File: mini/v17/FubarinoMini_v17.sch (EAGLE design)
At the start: 37 parts, among them IC1 AZ1117CR2-3.3TRG1, J1 M20, J2 M20, J8 USB-5PIN, Q1 8MHz, Q2 32.768 KHz, U1 PIC32MX270F256D_44QFN_44

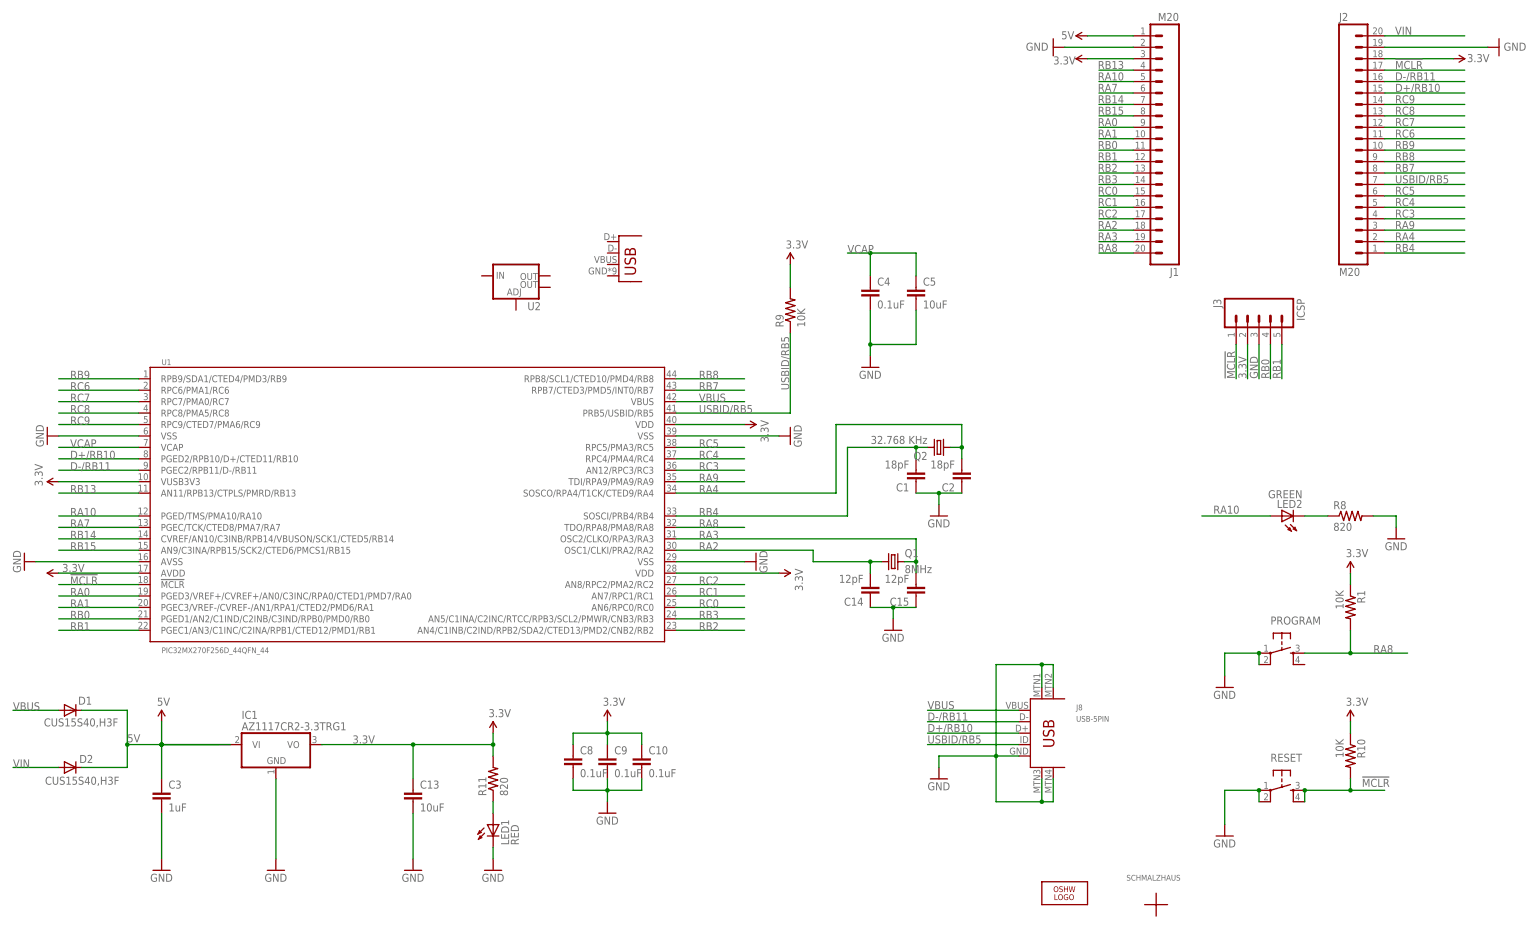
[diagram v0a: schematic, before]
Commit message: Version 2.0, first draft, done and sent to PCB fab. Changed switches, crystal, USB connector, rerouted most of board. Still need to rename folder to 2.0
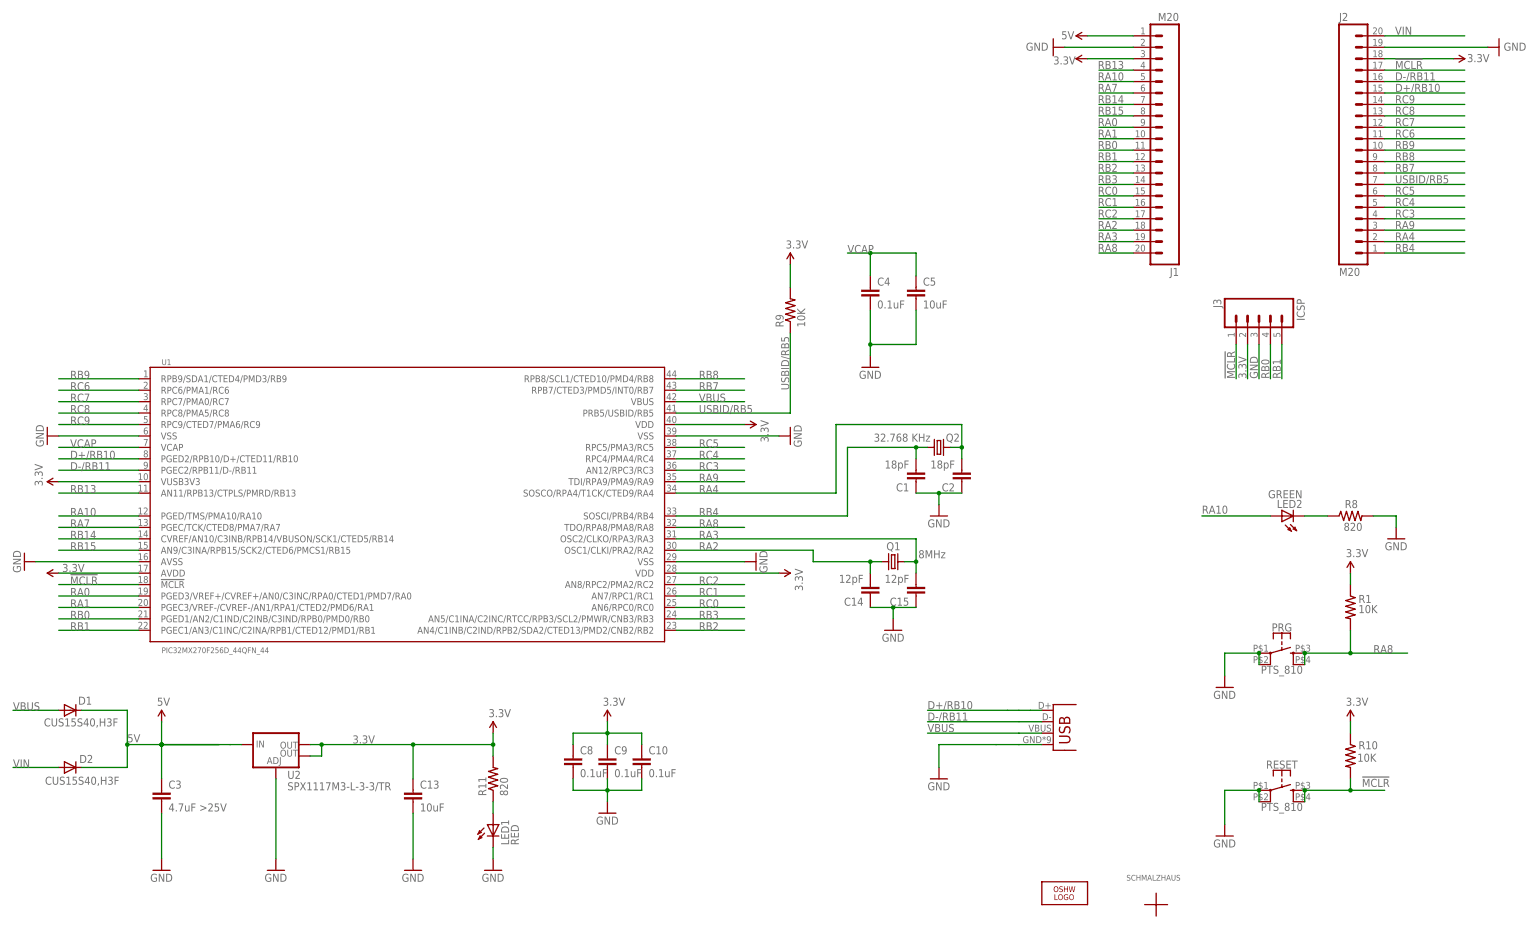
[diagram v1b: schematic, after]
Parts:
- removed IC1: AZ1117CR2-3.3TRG1, linear:MCP170333MB
- removed J8: USB-5PIN, SchmalzHaus:USB-5PIN
- removed PROGRAM: (no value), SparkFun02-20-08:TAC_SWITCHSND
- added PRG: PTS_810, CK_PTS_810_TactSwitch:PTS_810
- C3: value 1uF -> 4.7uF >25V
- Q1: device SchmalzHaus:CRYSTALNX5032 -> NDK_NX3225GD_Crystal:NX3225GD
- RESET: value (none) -> PTS_810; device SparkFun02-20-08:TAC_SWITCHSND -> CK_PTS_810_TactSwitch:PTS_810
- U2: value (none) -> SPX1117M3-L-3-3/TR
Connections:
- net 3.3V: now also U2.OUT, U2.OUT@1; no longer IC1.VO
- net 5V: now also U2.IN; no longer IC1.VI, IC1.VI1
- net D+/RB10: now also U$5.D+; no longer J8.D+
- net D-/RB11: now also U$5.D-; no longer J8.D-
- net GND: now also PRG.1, PRG.2, U$5.GND, U2.ADJ; no longer IC1.GND, J8.GND, J8.MTN1, J8.MTN2, J8.MTN3, J8.MTN4, PROGRAM.1, PROGRAM.2
- net RA8: now also PRG.3, PRG.4; no longer PROGRAM.3
- net USBID/RB5: no longer J8.ID
- net VBUS: now also U$5.VBUS; no longer J8.VBUS
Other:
- note added: "Arduino pin 1"
- note added: "Max 20V"
- note added: "Switched VBUS (pin 42) on micro to VBUS signal rather than 5V. Diodes switched to 1.5A max current LDO Reg switched to 800mA output, 20V max input CPU change to PIC32MX270F256D to get twice the Flash and RAM USB connector changed to Micro-B"
- note added: "USB Function (Micro B)"
- note added: "V1.7 07/18/2018"
- note removed: "Max 5.5V"
- note removed: "Switched VBUS (pin 42) on micro to VBUS signal rather than 5V. Diodes switched to 1.5A max current LDO Reg switched to 600mA output, 5.5V max input CPU change to PIC32MX270F256D to get twice the Flash and RAM"
- note removed: "USB Function (Mini B)"
- note removed: "V1.7 05/02/2018"
- moved on the sheet: U2
